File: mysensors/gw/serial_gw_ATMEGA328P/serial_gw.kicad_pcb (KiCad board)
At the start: 2 copper layers, 44.5 x 19.8 mm, 68 parts, among them CON1 AVR-ISP-6, IC1 ATMEGA328P-MU, P1 USB_A, P2 ANTENNA, SW1 RESET, U1 TXB0104, U2 MCP1703A-3302, U3 CP2102, U4 RFM69W, U5 ATSHA204A, X1 16MHz

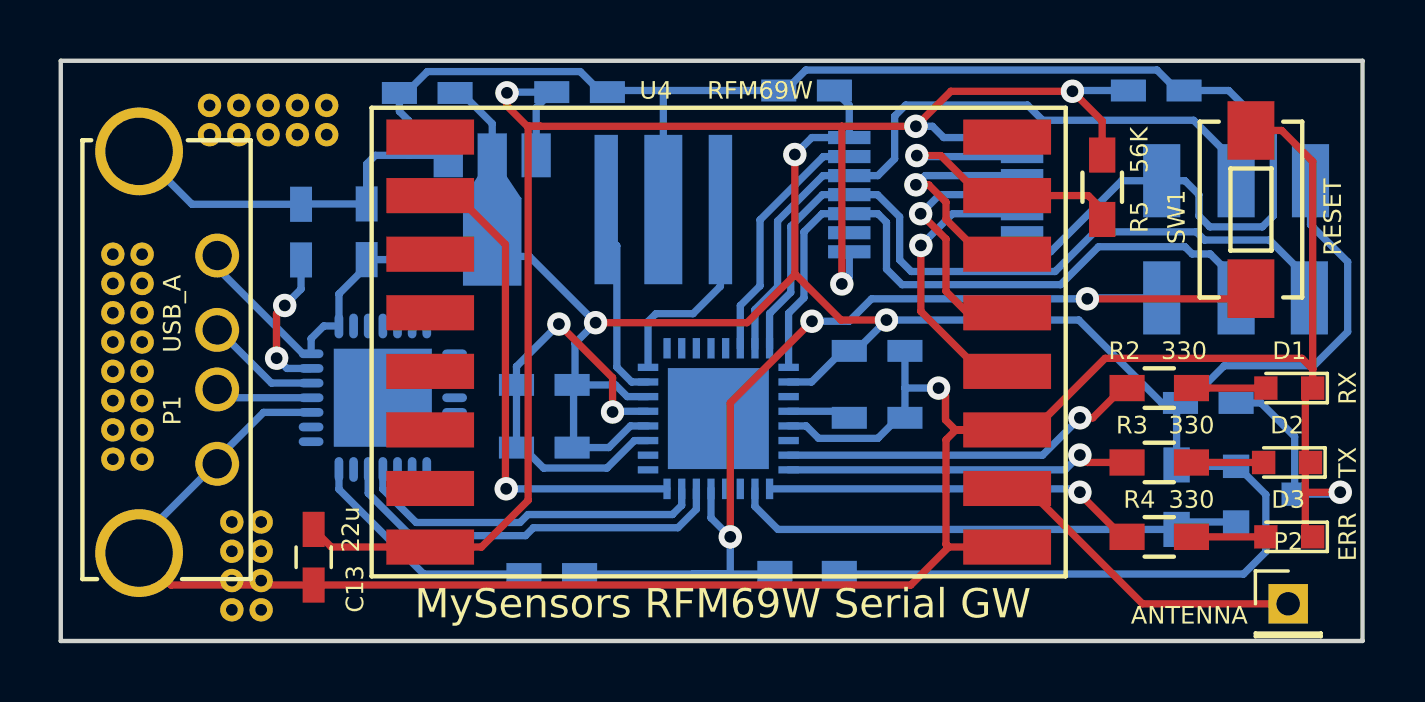
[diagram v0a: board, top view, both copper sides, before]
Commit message: [mysensors serial_gw_ATMEGA328P] added ferrite bead for EMI suppression
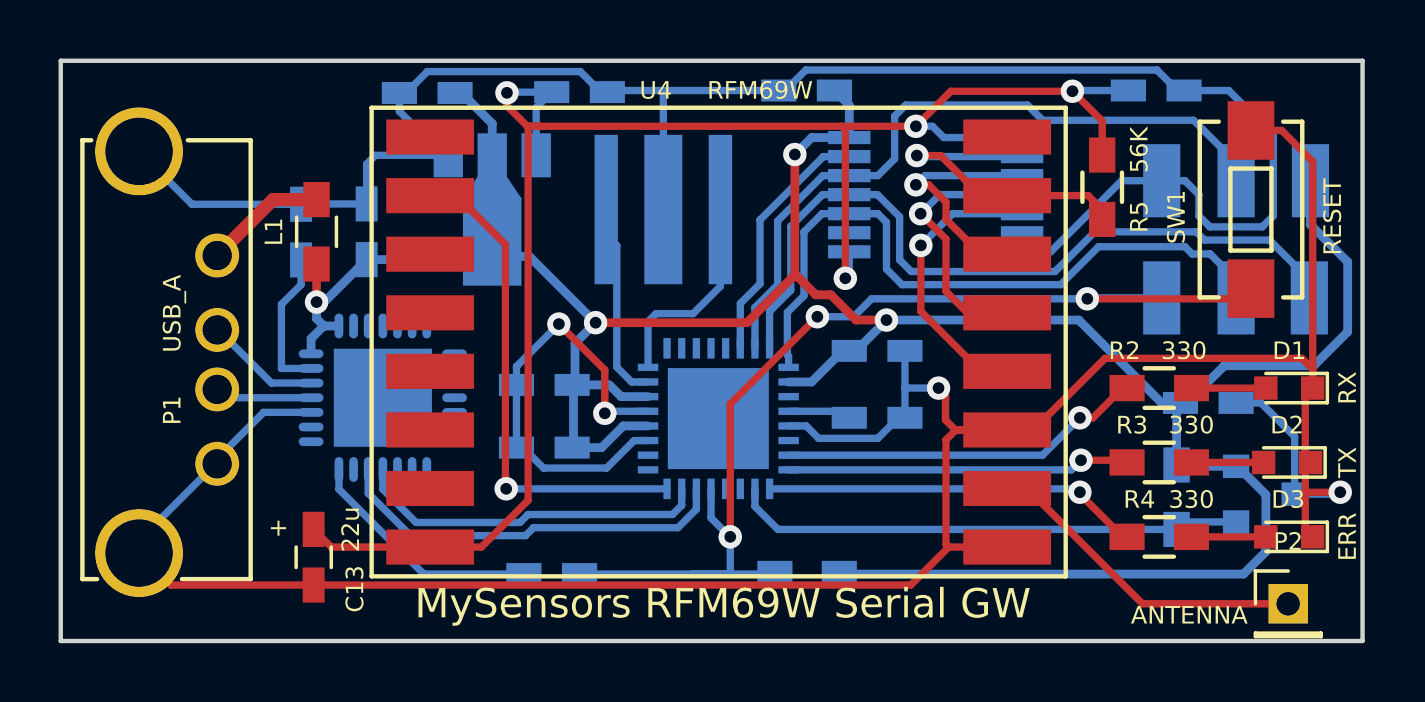
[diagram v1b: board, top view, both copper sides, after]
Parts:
- removed REF** (x34): 1pin, myfootprints:1pin
- added L1: BLM18HE152SN1D, Resistors_SMD:R_0603_HandSoldering, F.Cu at (79.6, 79.5)
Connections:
- P1 pad 1: +5V -> Net-(L1-Pad2)
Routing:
- net Net-(L1-Pad2): track 0.00 -> 4.60 mm
- net +5V: track 106.1 -> 103.4 mm, vias 3 -> 4
- net Net-(C12-Pad1): track 5.03 -> 5.00 mm, vias 2 -> 0
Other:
- board text added: "+"
- board text added: "Rev. 0.4"
- board text removed: "Rev. 0.3"
